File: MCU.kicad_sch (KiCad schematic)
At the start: 41 parts, among them J1 JTAG, J2 HH-16P-CB-TYPE-C, J3 GPS, J4 CAM, J5 GPS, J6 CAM, SW1 TS2306A, U4 RP2354A, U5 W25Q128JVPIQ, U6 USBLC6-2P6, Y1 40MHz

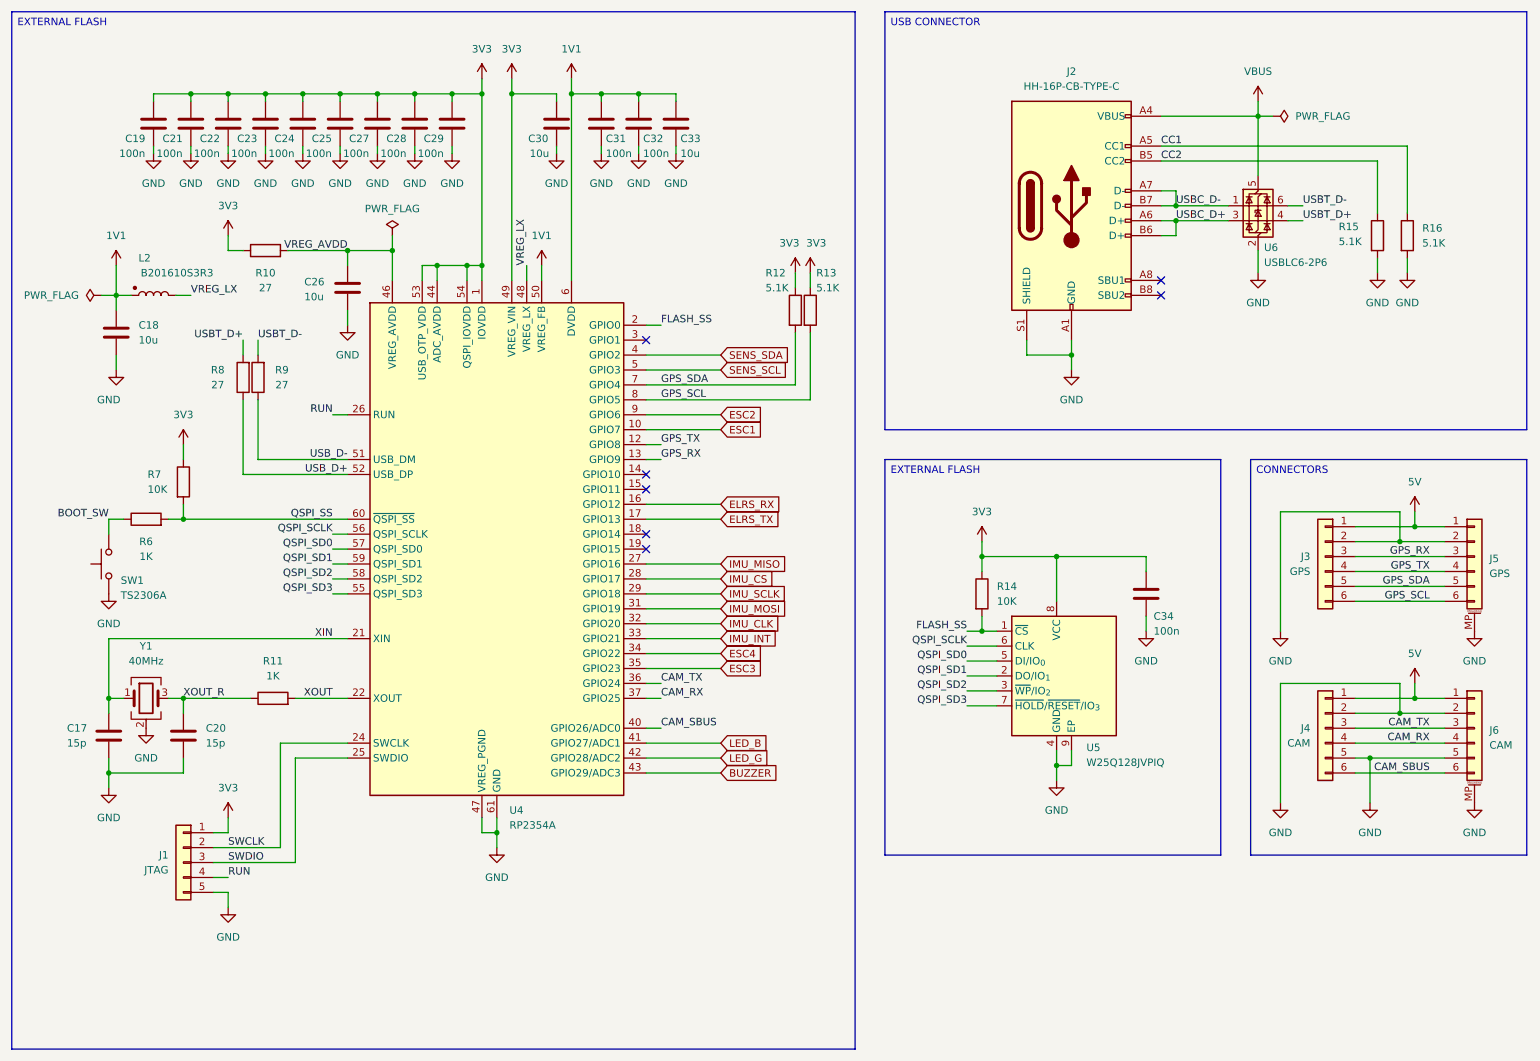
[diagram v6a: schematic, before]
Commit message: Schematic and PCB
Reviewed the schematic and deleted unused components.
Updated the PCB and also removed unused footprints.
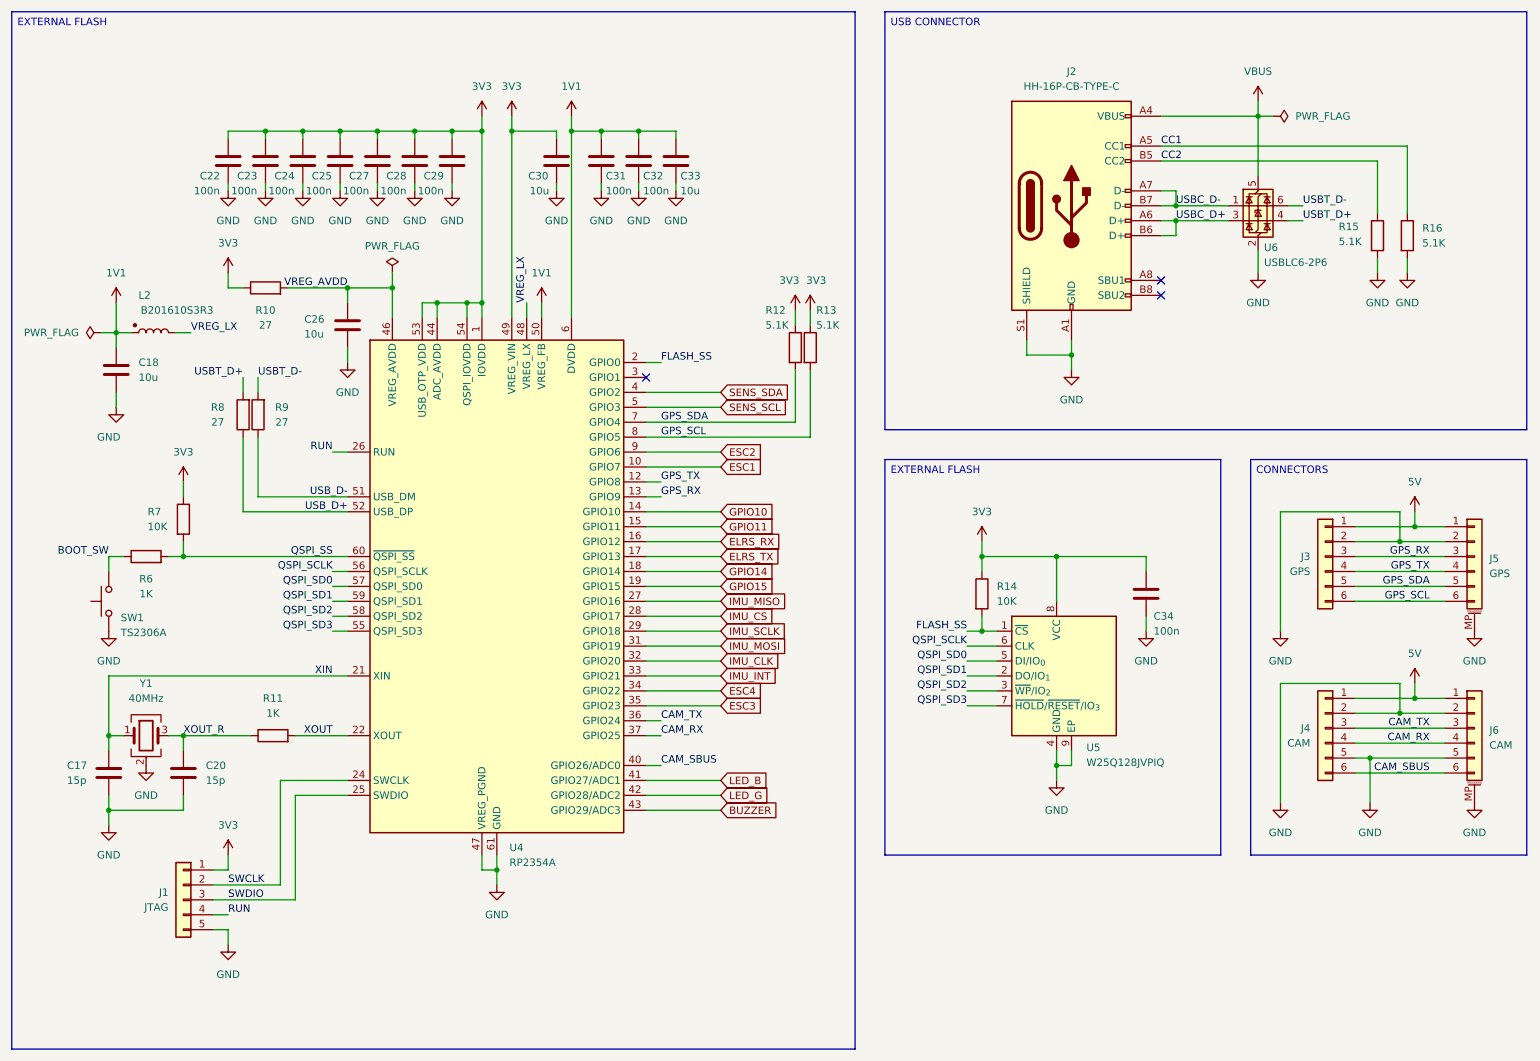
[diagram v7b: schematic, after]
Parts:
- removed C19, C21: 100n, Capacitor_SMD:C_0603_1608Metric, symbol Device:C
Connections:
- net GPIO10: now reaches U4.14 (GPIO10)
- net GPIO11: now reaches U4.15 (GPIO11)
- net GPIO14: now reaches U4.18 (GPIO14)
- net GPIO15: now reaches U4.19 (GPIO15)
- no-connect marks 7 -> 3
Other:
- moved on the sheet: C17, C18, C20, C22, C23, C24, C25, C26, C27, C28, C29, C30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

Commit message: IMU filtering and layout
Added a missing capacitor for the IMU.
Updated the PCB layout.
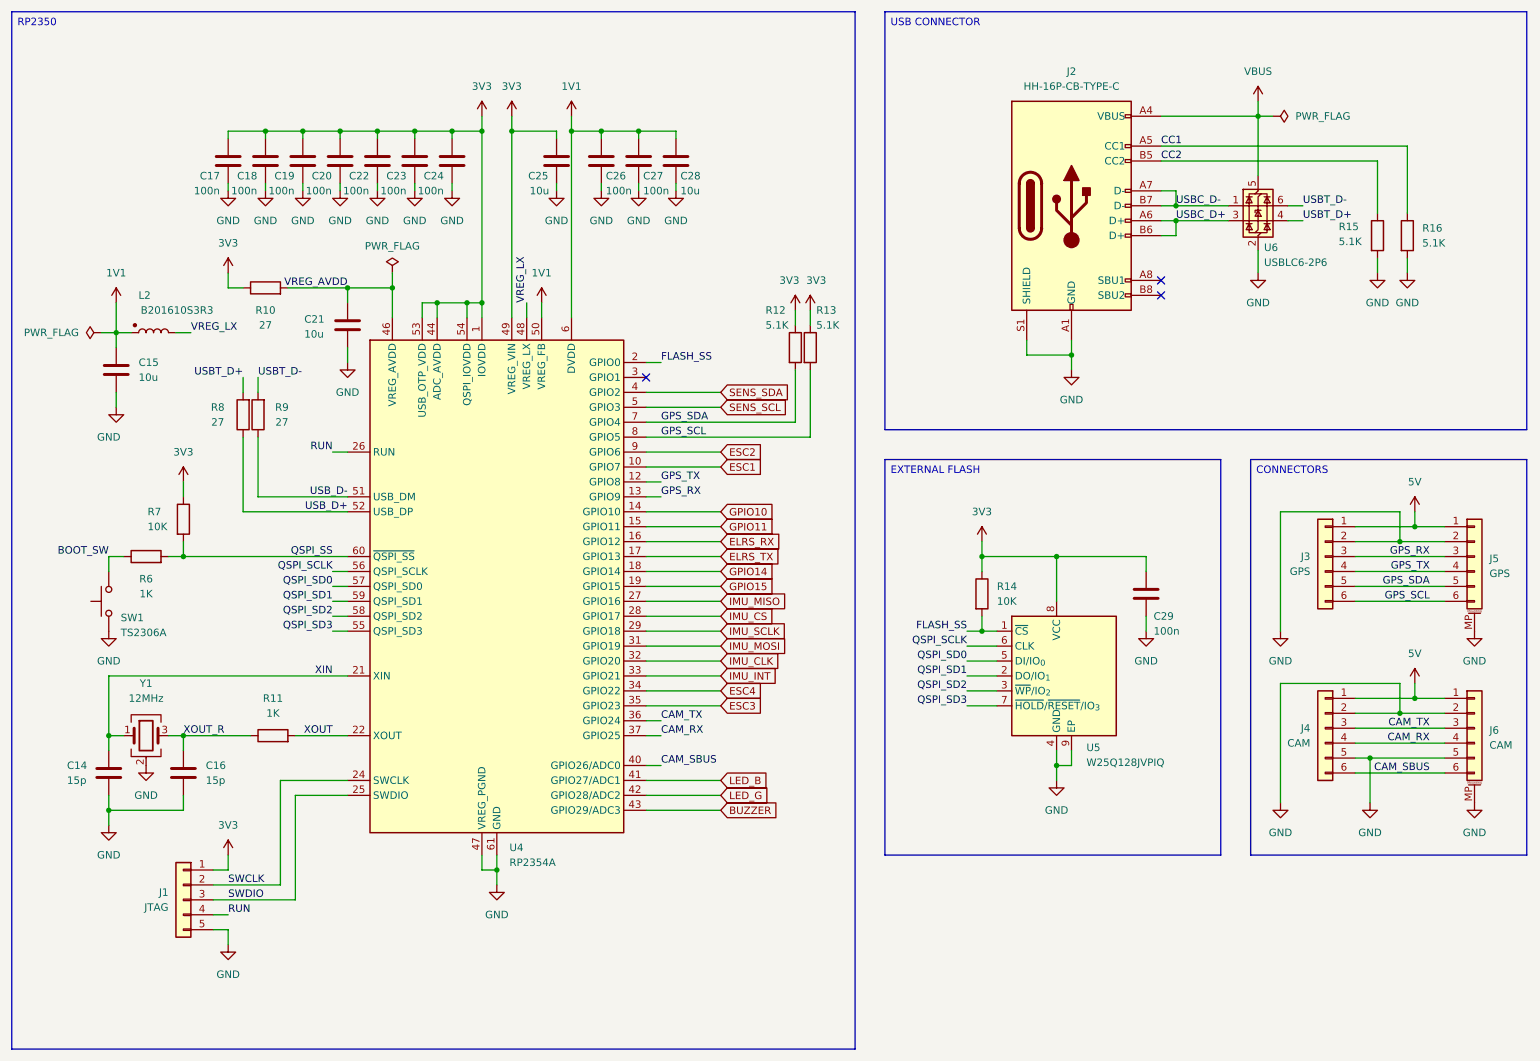
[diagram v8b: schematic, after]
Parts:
- Y1: value 40MHz -> 12MHz
- renumbered C17 to C14, C18 to C15, C20 to C16, C22 to C17, C23 to C18, C24 to C19, C25 to C20, C26 to C21, C27 to C22, C28 to C23, C29 to C24, C30 to C25, C31 to C26, C32 to C27, C33 to C28, C34 to C29
